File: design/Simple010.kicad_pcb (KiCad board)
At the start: 4 copper layers, 100 x 100 mm, 75 parts, among them J1 CS2, J2 Conn_02x05_Odd_Even, J3 USB_C_Receptacle_USB2.0_16P, J4 Backup serial, J7 Conn_02x32_Odd_Even, J8 SD Card, SW1 Reset, U1 MCP2221A, U10 MC68010P, U11 UM809SS, U14 SST39SF040, U15 SST39SF040, U16 AS6C4008-55PCN, U17 AS6C4008-55PCN, U2 ATF1508ASx-xxJx84, U9 USBLC6-2SC6, Y3 SG-5032CAN 3.6864MHz, Y4 SG-5032CAN 10MHz

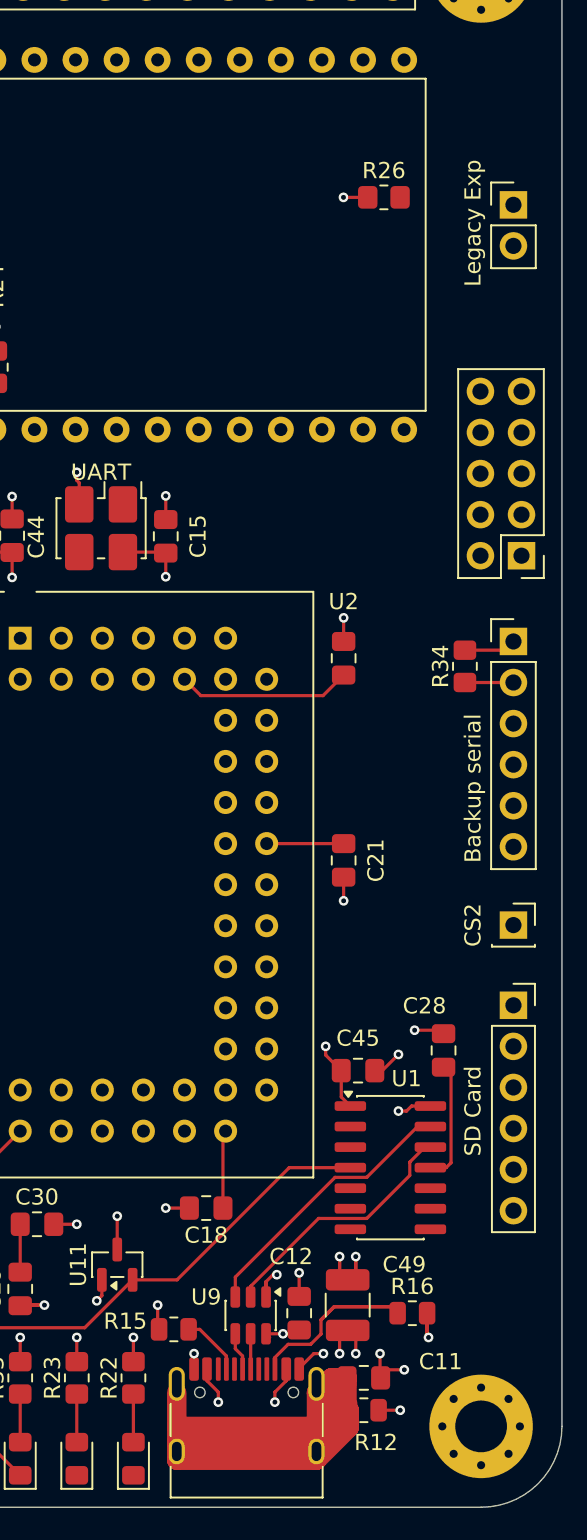
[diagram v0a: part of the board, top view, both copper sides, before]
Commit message: Fix all R/C part numbers: switch to JLCPCB basic parts, correct footprints
- Replace all non-basic LCSC numbers with JLCPCB basic equivalents (no
  extended part setup fees): Samsung MLCCs for caps, UNI-ROYAL 0805W8F
  series for resistors
- Fix C49 footprint: 1210 → 1206 to match Samsung CL31A476MPHNNNE
- Correct previously wrong LCSC numbers (C17512→C17513, C17515→C17673,
  C135808→C96123) and missing R17 part numbers
- Update all Mouser numbers to match the LCSC manufacturer throughout
- Standardise all resistor footprints to HandSolder pad variant
- Update datasheets/INDEX.md with verified basic part table

Co-Authored-By: Claude Sonnet 4.6 <noreply@anthropic.com>
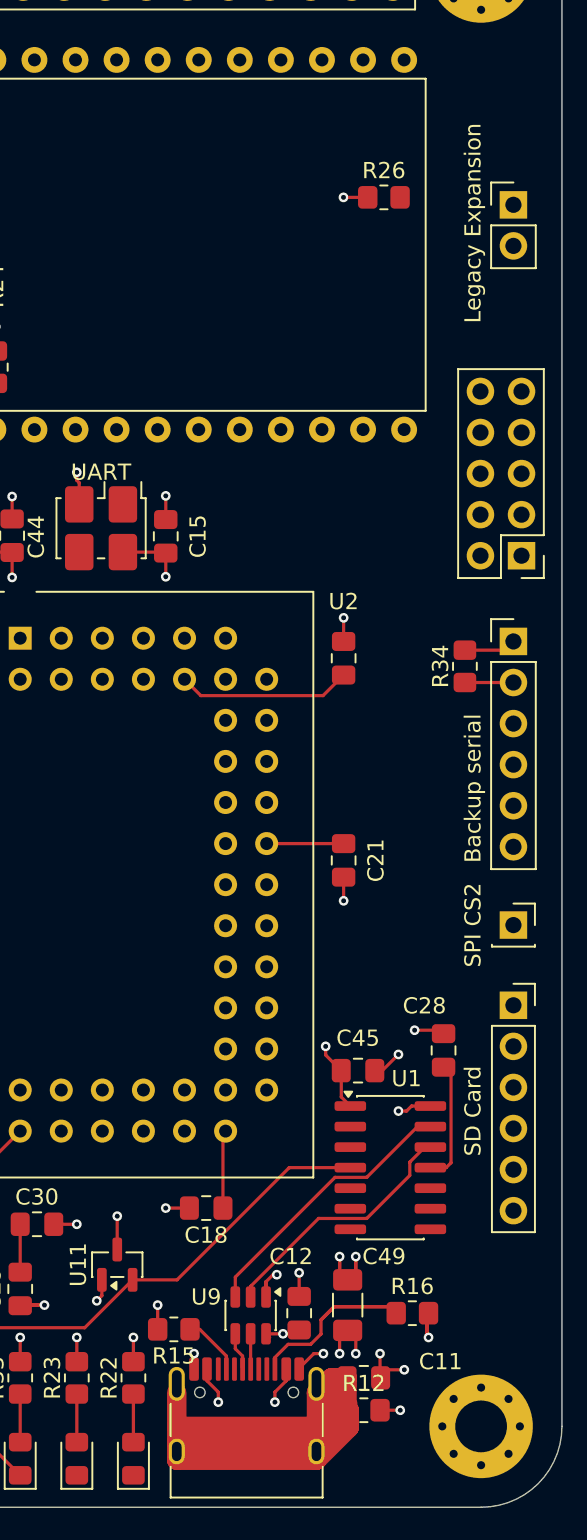
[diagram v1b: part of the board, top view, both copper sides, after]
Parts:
- C49: footprint Capacitor_SMD:C_1210_3225Metric_Pad1.33x2.70mm_HandSolder -> Capacitor_SMD:C_1206_3216Metric_Pad1.33x1.80mm_HandSolder
- J1: value CS2 -> SPI CS2
- JP2: value Legacy Exp -> Legacy Expansion
- R12, R15, R16: footprint Resistor_SMD:R_0805_2012Metric -> Resistor_SMD:R_0805_2012Metric_Pad1.20x1.40mm_HandSolder
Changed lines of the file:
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@@
 			)
 		)
-		(property "LCSC" "C17515"
+		(property "LCSC" "C17673"
 			(at 0 0 270)
 			(unlocked yes)
@@
 			)
 		)
-		(property "LCSC" "C17515"
+		(property "LCSC" "C17673"
 			(at 0 0 90)
 			(unlocked yes)
@@
 		)
 	)
-	(footprint "Capacitor_SMD:C_1210_3225Metric_Pad1.33x2.70mm_HandSolder"
+	(footprint "Capacitor_SMD:C_1206_3216Metric_Pad1.33x1.80mm_HandSolder"
 		(layer "F.Cu")
 		(at 141.75 142.5 90)
-		(descr "Capacitor SMD 1210 (3225 Metric), square (rectangular) end terminal, IPC-7351 nominal with elongated pad for handsoldering. (Body size source: IPC-SM-782 page 76, https://www.pcb-3d.com/wordpress/wp-content/uploads/ipc-sm-782a_amendment_1_and_2.pdf)")
+		(descr "Capacitor SMD 1206 (3216 Metric), square (rectangular) end terminal, IPC-7351 nominal with elongated pad for handsoldering. (Body size source: IPC-SM-782 page 76, https://www.pcb-3d.com/wordpress/wp-content/uploads/ipc-sm-782a_amendment_1_and_2.pdf)")
 		(tags "capacitor handsolder")
 		(property "Reference" "C49"
-			(at 2.5 3.5 180)
+			(at 3 2.25 180)
 			(layer "F.SilkS")
 			(effects
@@
 		)
 		(property "Value" "47uF"
-			(at 0 2.3 90)
+			(at 0 1.85 90)
 			(layer "F.Fab")
 			(hide yes)
@@
 			)
 		)
-		(property "LCSC" "C135808"
+		(property "LCSC" "C96123"
 			(at 0 0 90)
 			(unlocked yes)
@@
 			)
 		)
-		(property "Mouser" "J32MLB7476MPPDTJ"
+		(property "Mouser" "187-CL31A476MPHNNNE"
 			(at 0 0 90)
 			(unlocked yes)
@@
 		(duplicate_pad_numbers_are_jumpers no)
 		(fp_line
-			(start -0.711252 -1.36)
-			(end 0.711252 -1.36)
+			(start -0.711252 -0.91)
+			(end 0.711252 -0.91)
 			(stroke
 				(width 0.12)
@@
 		)
 		(fp_line
-			(start -0.711252 1.36)
-			(end 0.711252 1.36)
+			(start -0.711252 0.91)
+			(end 0.711252 0.91)
 			(stroke
 				(width 0.12)
@@
 		)
 		(fp_rect
-			(start -2.48 -1.6)
-			(end 2.48 1.6)
+			(start -2.48 -1.15)
+			(end 2.48 1.15)
 			(stroke
 				(width 0.05)
@@
 		)
 		(fp_rect
-			(start -1.6 -1.25)
-			(end 1.6 1.25)
+			(start -1.6 -0.8)
+			(end 1.6 0.8)
 			(stroke
 				(width 0.1)
@@
 		(pad "1" smd roundrect
 			(at -1.5625 0 90)
-			(size 1.325 2.7)
+			(size 1.325 1.8)
 			(layers "F.Cu" "F.Mask" "F.Paste")
 			(roundrect_rratio 0.188679)
@@
 		(pad "2" smd roundrect
 			(at 1.5625 0 90)
-			(size 1.325 2.7)
+			(size 1.325 1.8)
 			(layers "F.Cu" "F.Mask" "F.Paste")
 			(roundrect_rratio 0.188679)
@@
 		)
 		(embedded_fonts no)
-		(model "${KICAD10_3DMODEL_DIR}/Capacitor_SMD.3dshapes/C_1210_3225Metric.step"
+		(model "${KICAD10_3DMODEL_DIR}/Capacitor_SMD.3dshapes/C_1206_3216Metric.step"
 			(offset
 				(xyz 0 0 0)
@@
 			)
 		)
-		(property "LCSC" "C17515"
+		(property "LCSC" "C17673"
 			(at 0 0 0)
 			(unlocked yes)
@@
 			)
 		)
-		(property "LCSC" "C17512"
+		(property "LCSC" "C17379"
 			(at 0 0 270)
 			(unlocked yes)
@@
 			)
 		)
-		(property "LCSC" "C17515"
+		(property "LCSC" "C17673"
 			(at 0 0 90)
 			(unlocked yes)
@@
 			)
 		)
-		(property "LCSC" "C17515"
+		(property "LCSC" "C17673"
 			(at 0 0 180)
 			(unlocked yes)
@@
 			)
 		)
-		(property "LCSC" "C17515"
+		(property "LCSC" "C17673"
 			(at 0 0 270)
 			(unlocked yes)
@@
 			)
 		)
-		(property "LCSC" "C17515"
+		(property "LCSC" "C17673"
 			(at 0 0 270)
 			(unlocked yes)
@@
 			)
 		)
-		(property "Mouser" ""
+		(property "Mouser" "ERJ-6ENF1001V"
 			(at 0 0 180)
 			(unlocked yes)
@@
 			)
 		)
-		(property "LCSC" ""
+		(property "LCSC" "C17513"
 			(at 0 0 180)
 			(unlocked yes)
@@
 			)
 		)
-		(property "LCSC" "C17512"
+		(property "LCSC" "C17513"
 			(at 0 0 270)
 			(unlocked yes)
@@
 			)
 		)
-		(property "Value" "CS2"
+		(property "Value" "SPI CS2"
 			(at -2.5 0 90)
 			(layer "F.SilkS")
@@
 		)
 	)
-	(footprint "Resistor_SMD:R_0805_2012Metric"
+	(footprint "Resistor_SMD:R_0805_2012Metric_Pad1.20x1.40mm_HandSolder"
 		(layer "F.Cu")
 		(at 131 144 180)
-		(descr "Resistor SMD 0805 (2012 Metric), square (rectangular) end terminal, IPC-7351 nominal, (Body size source: IPC-SM-782 page 72, https://www.pcb-3d.com/wordpress/wp-content/uploads/ipc-sm-782a_amendment_1_and_2.pdf)")
-		(tags "resistor")
+		(descr "Resistor SMD 0805 (2012 Metric), square (rectangular) end terminal, IPC-7351 nominal with elongated pad for handsoldering. (Body size source: IPC-SM-782 page 72, https://www.pcb-3d.com/wordpress/wp-content/uploads/ipc-sm-782a_amendment_1_and_2.pdf)")
+		(tags "resistor handsolder")
 		(property "Reference" "R15"
-			(at 3 0.5 0)
+			(at 0 -1.65 180)
 			(layer "F.SilkS")
 			(effects
@@
 		)
 		(property "Value" "5.1k"
-			(at 0 1.65 0)
+			(at 0 1.65 180)
 			(layer "F.Fab")
 			(hide yes)
@@
 		)
 		(property "Datasheet" ""
-			(at 0 0 0)
+			(at 0 0 180)
 			(layer "F.Fab")
 			(hide yes)
@@
 		)
 		(property "Description" ""
-			(at 0 0 0)
+			(at 0 0 180)
 			(layer "F.Fab")
 			(hide yes)
@@
 		)
 		(property "KiLib_Generator" "SMD_2terminal_chip_molded"
-			(at 0 0 0)
+			(at 0 0 180)
 			(layer "F.SilkS")
 			(hide yes)
@@
 		)
 		(fp_rect
-			(start -1.68 -0.95)
-			(end 1.68 0.95)
+			(start -1.85 -0.95)
+			(end 1.85 0.95)
 			(stroke
 				(width 0.05)
@@
 		)
 		(fp_text user "${REFERENCE}"
-			(at 0 0 0)
+			(at 0 0 180)
 			(layer "F.Fab")
 			(effects
@@
 		)
 		(pad "1" smd roundrect
-			(at -0.9125 0 180)
-			(size 1.025 1.4)
+			(at -1 0 180)
+			(size 1.2 1.4)
 			(layers "F.Cu" "F.Mask" "F.Paste")
-			(roundrect_rratio 0.243902)
+			(roundrect_rratio 0.208333)
 			(net "Net-(J3-CC1)")
 			(pintype "passive")
 		)
 		(pad "2" smd roundrect
-			(at 0.9125 0 180)
-			(size 1.025 1.4)
+			(at 1 0 180)
+			(size 1.2 1.4)
 			(layers "F.Cu" "F.Mask" "F.Paste")
-			(roundrect_rratio 0.243902)
+			(roundrect_rratio 0.208333)
 			(net "GND")
 			(pintype "passive")
@@
 		)
 	)
-	(footprint "Resistor_SMD:R_0805_2012Metric"
+	(footprint "Resistor_SMD:R_0805_2012Metric_Pad1.20x1.40mm_HandSolder"
 		(layer "F.Cu")
 		(at 142.75 149)
-		(descr "Resistor SMD 0805 (2012 Metric), square (rectangular) end terminal, IPC-7351 nominal, (Body size source: IPC-SM-782 page 72, https://www.pcb-3d.com/wordpress/wp-content/uploads/ipc-sm-782a_amendment_1_and_2.pdf)")
-		(tags "resistor")
+		(descr "Resistor SMD 0805 (2012 Metric), square (rectangular) end terminal, IPC-7351 nominal with elongated pad for handsoldering. (Body size source: IPC-SM-782 page 72, https://www.pcb-3d.com/wordpress/wp-content/uploads/ipc-sm-782a_amendment_1_and_2.pdf)")
+		(tags "resistor handsolder")
 		(property "Reference" "R12"
-			(at 0.75 2 0)
+			(at 0 -1.65 0)
 			(layer "F.SilkS")
 			(effects
@@
 		)
 		(fp_rect
-			(start -1.68 -0.95)
-			(end 1.68 0.95)
+			(start -1.85 -0.95)
+			(end 1.85 0.95)
 			(stroke
 				(width 0.05)
@@
 		)
 		(pad "1" smd roundrect
-			(at -0.9125 0)
-			(size 1.025 1.4)
+			(at -1 0)
+			(size 1.2 1.4)
 			(layers "F.Cu" "F.Mask" "F.Paste")
-			(roundrect_rratio 0.243902)
+			(roundrect_rratio 0.208333)
 			(net "GNDS")
 			(pintype "passive")
 		)
 		(pad "2" smd roundrect
-			(at 0.9125 0)
-			(size 1.025 1.4)
+			(at 1 0)
+			(size 1.2 1.4)
 			(layers "F.Cu" "F.Mask" "F.Paste")
-			(roundrect_rratio 0.243902)
+			(roundrect_rratio 0.208333)
 			(net "GND")
 			(pintype "passive")
@@
 		)
 	)
-	(footprint "Resistor_SMD:R_0805_2012Metric"
+	(footprint "Resistor_SMD:R_0805_2012Metric_Pad1.20x1.40mm_HandSolder"
 		(layer "F.Cu")
 		(at 145.75 143)
-		(descr "Resistor SMD 0805 (2012 Metric), square (rectangular) end terminal, IPC-7351 nominal, (Body size source: IPC-SM-782 page 72, https://www.pcb-3d.com/wordpress/wp-content/uploads/ipc-sm-782a_amendment_1_and_2.pdf)")
-		(tags "resistor")
+		(descr "Resistor SMD 0805 (2012 Metric), square (rectangular) end terminal, IPC-7351 nominal with elongated pad for handsoldering. (Body size source: IPC-SM-782 page 72, https://www.pcb-3d.com/wordpress/wp-content/uploads/ipc-sm-782a_amendment_1_and_2.pdf)")
+		(tags "resistor handsolder")
 		(property "Reference" "R16"
 			(at 0 -1.65 0)
@@
 		)
 		(fp_rect
-			(start -1.68 -0.95)
-			(end 1.68 0.95)
+			(start -1.85 -0.95)
+			(end 1.85 0.95)
 			(stroke
 				(width 0.05)
@@
 		)
 		(pad "1" smd roundrect
-			(at -0.9125 0)
-			(size 1.025 1.4)
+			(at -1 0)
+			(size 1.2 1.4)
 			(layers "F.Cu" "F.Mask" "F.Paste")
-			(roundrect_rratio 0.243902)
+			(roundrect_rratio 0.208333)
 			(net "Net-(J3-CC2)")
 			(pintype "passive")
 		)
 		(pad "2" smd roundrect
-			(at 0.9125 0)
-			(size 1.025 1.4)
+			(at 1 0)
+			(size 1.2 1.4)
 			(layers "F.Cu" "F.Mask" "F.Paste")
-			(roundrect_rratio 0.243902)
+			(roundrect_rratio 0.208333)
 			(net "GND")
 			(pintype "passive")
@@
 			)
 		)
-		(property "LCSC" "C17515"
+		(property "LCSC" "C17673"
 			(at 0 0 270)
 			(unlocked yes)
@@
 			)
 		)
-		(property "LCSC" "C17515"
+		(property "LCSC" "C17673"
 			(at 0 0 90)
 			(unlocked yes)
@@
 			)
 		)
-		(property "LCSC" "C17515"
+		(property "LCSC" "C17673"
 			(at 0 0 270)
 			(unlocked yes)
@@
 			)
 		)
-		(property "Value" "Legacy Exp"
+		(property "Value" "Legacy Expansion"
 			(at -2.5 1.135 90)
 			(layer "F.SilkS")
@@
 			)
 		)
-		(property "LCSC" "C17515"
+		(property "LCSC" "C17673"
 			(at 0 0 270)
 			(unlocked yes)
@@
 			)
 		)
-		(property "LCSC" "C17515"
+		(property "LCSC" "C17673"
 			(at 0 0 270)
 			(unlocked yes)
@@
 			)
 		)
-		(property "LCSC" "C17515"
+		(property "LCSC" "C17673"
 			(at 0 0 90)
 			(unlocked yes)
@@
 			)
 		)
-		(property "LCSC" "C17512"
+		(property "LCSC" "C17513"
 			(at 0 0 270)
 			(unlocked yes)
@@
 			)
 		)
-		(property "Mouser" "649-10118192-0001LF"
+		(property "Mouser" "649-10171746-00021LF"
 			(at 0 0 0)
 			(unlocked yes)
@@
 			)
 		)
-		(property "LCSC" "C230736"
+		(property "LCSC" "C165948"
 			(at 0 0 0)
 			(unlocked yes)

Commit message: Fix even/odd memory bus wiring and route PCB
- Connect U15 (even ROM) and U17 (even RAM) data pins to D8-D15 instead
  of D0-D7: upper byte was completely unconnected, causing half-garbage
  reads and lost writes on all 16-bit accesses
- Reduce R32/R33 LED resistors from 4.7k to 1k (MCP2221A GPIO is 3.3V,
  4.7k gave only 0.26mA — too dim)
- Initial PCB layout and routing

Co-Authored-By: Claude Sonnet 4.6 <noreply@anthropic.com>
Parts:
- J1: value SPI CS2 -> CS2
- R17: value 1k -> 1K
- R19, R20: value 10k -> 10K
- R32, R33: value 4K7 -> 1K
- U11: value UM809SS -> LM809M3-4.63/NOPB
- moved C15 22.3 mm to (147.5, 109.5)
- moved Y3 22.3 mm to (143.5, 109.0)
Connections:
- U15 pad 13: D0 -> D8
- U15 pad 14: D1 -> D9
- U15 pad 15: D2 -> D10
- U15 pad 17: D3 -> D11
- U15 pad 18: D4 -> D12
- U15 pad 19: D5 -> D13
- U15 pad 20: D6 -> D14
- U15 pad 21: D7 -> D15
- U17 pad 13: D0 -> D8
- U17 pad 14: D1 -> D9
- U17 pad 15: D2 -> D10
- U17 pad 17: D3 -> D11
- U17 pad 18: D4 -> D12
- U17 pad 19: D5 -> D13
- U17 pad 20: D6 -> D14
- U17 pad 21: D7 -> D15
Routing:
- net A4: track 0.00 -> 239.2 mm, vias 0 -> 2
- net A7: track 0.00 -> 234.7 mm, vias 0 -> 3
- net A8: track 0.00 -> 227.1 mm, vias 0 -> 5
- net A3: track 0.00 -> 224.7 mm, vias 0 -> 3
- net A1: track 0.00 -> 218.1 mm, vias 0 -> 8
- net A6: track 0.00 -> 213.7 mm, vias 0 -> 5
- net A19: track 0.00 -> 210.8 mm, vias 0 -> 4
- net A2: track 0.00 -> 210.7 mm, vias 0 -> 2
- net A12: track 0.00 -> 209.7 mm, vias 0 -> 3
- net A5: track 0.00 -> 207.8 mm, vias 0 -> 2
- net A16: track 0.00 -> 201.5 mm, vias 0 -> 6
- net A10: track 0.00 -> 201.4 mm, vias 0 -> 3
- net A13: track 0.00 -> 196.5 mm, vias 0 -> 1
- net A17: track 0.00 -> 193.0 mm, vias 0 -> 5
- net A18: track 0.64 -> 190.5 mm, vias 0 -> 2
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
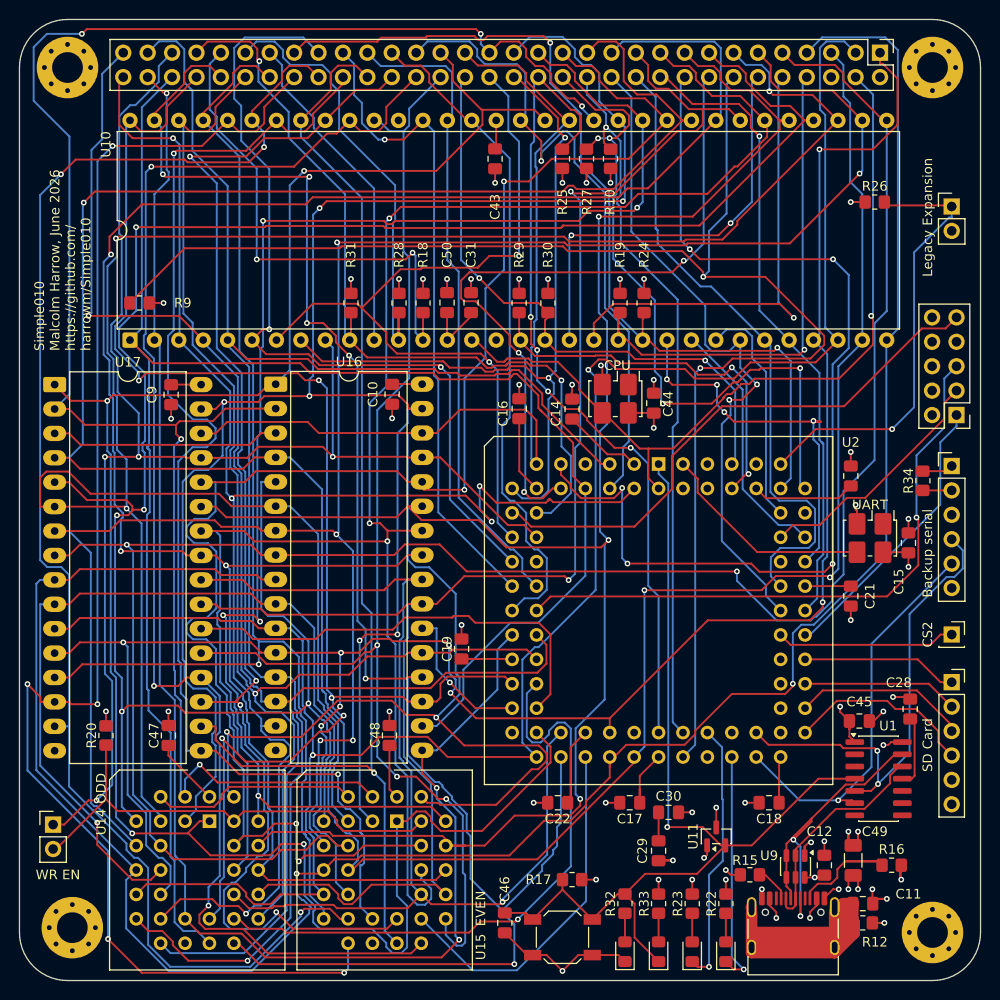
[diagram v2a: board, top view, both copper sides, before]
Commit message: Update KiCad design files and add fabrication outputs
Schematic and PCB updates including component renumbering (ICs, passives,
LEDs, oscillators). Add JLCPCB fabrication toolkit settings and v1
production outputs (gerbers zip, IPC netlist).

Co-Authored-By: Claude Sonnet 4.6 <noreply@anthropic.com>
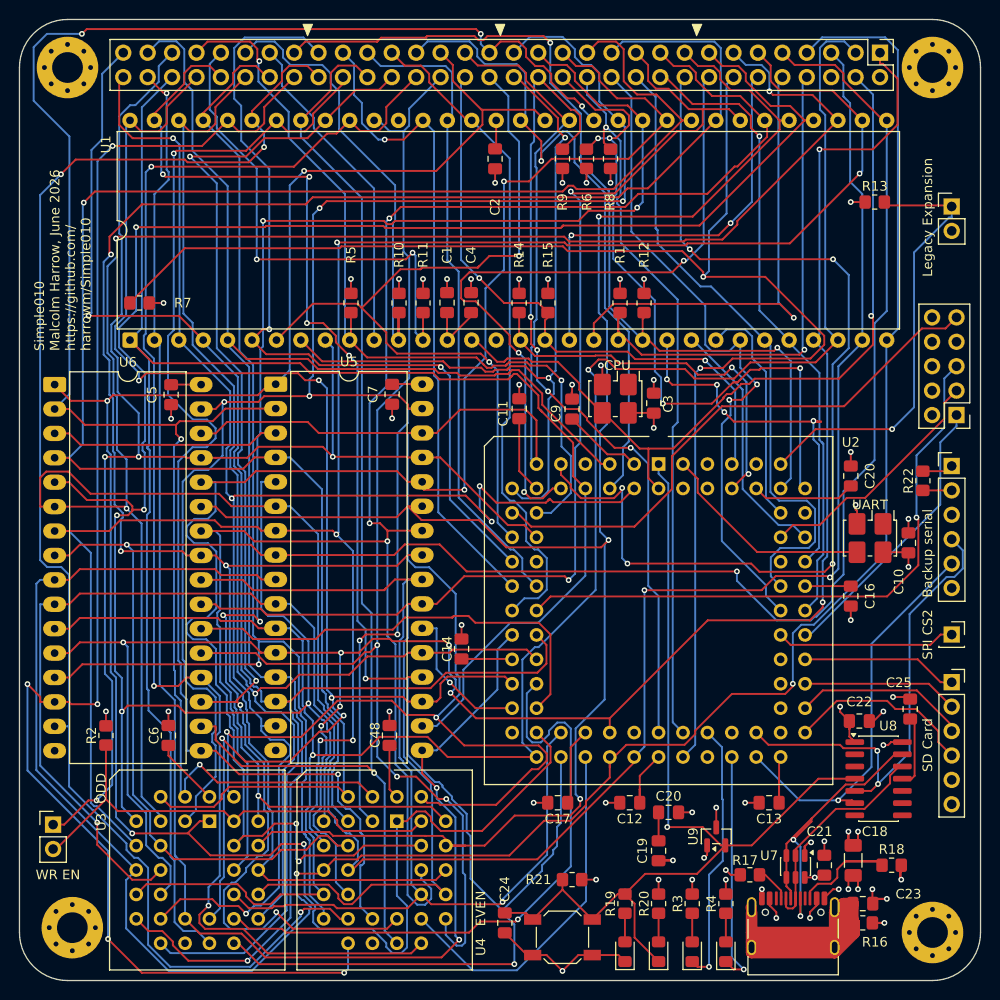
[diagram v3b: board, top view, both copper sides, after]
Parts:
- J1: value CS2 -> SPI CS2
- renumbered C50 to C1, C15 to C10, C16 to C11, C17 to C12, C18 to C13, C19 to C14, C20 to C15, C21 to C16, C22 to C17, C49 to C18, C29 to C19, C43 to C2, C30 to C20, C12 to C21, C45 to C22, C11 to C23, C46 to C24, C28 to C25, C44 to C3, C31 to C4, C9 to C5, C47 to C6, C10 to C7, C48 to C8, C14 to C9, LED9 to LED1, LED10 to LED2, LED1 to LED3, LED2 to LED4, R19 to R1, R28 to R10, R18 to R11, R24 to R12, R26 to R13, R29 to R14, R30 to R15, R12 to R16, R15 to R17, R16 to R18, R32 to R19, R20 to R2, R33 to R20, R17 to R21, R34 to R22, R23 to R3, R22 to R4, R31 to R5, R27 to R6, R9 to R7, R10 to R8, R25 to R9, U10 to U1, U14 to U3, U15 to U4, U16 to U5, U17 to U6, U9 to U7, U1 to U8, U11 to U9, Y4 to Y1, Y3 to Y2
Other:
- board text added: "C20"
